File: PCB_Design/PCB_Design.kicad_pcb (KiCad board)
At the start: 2 copper layers, 1 part, among them IC1 ESP32-WROOM-32_M103QH3200PH3Q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

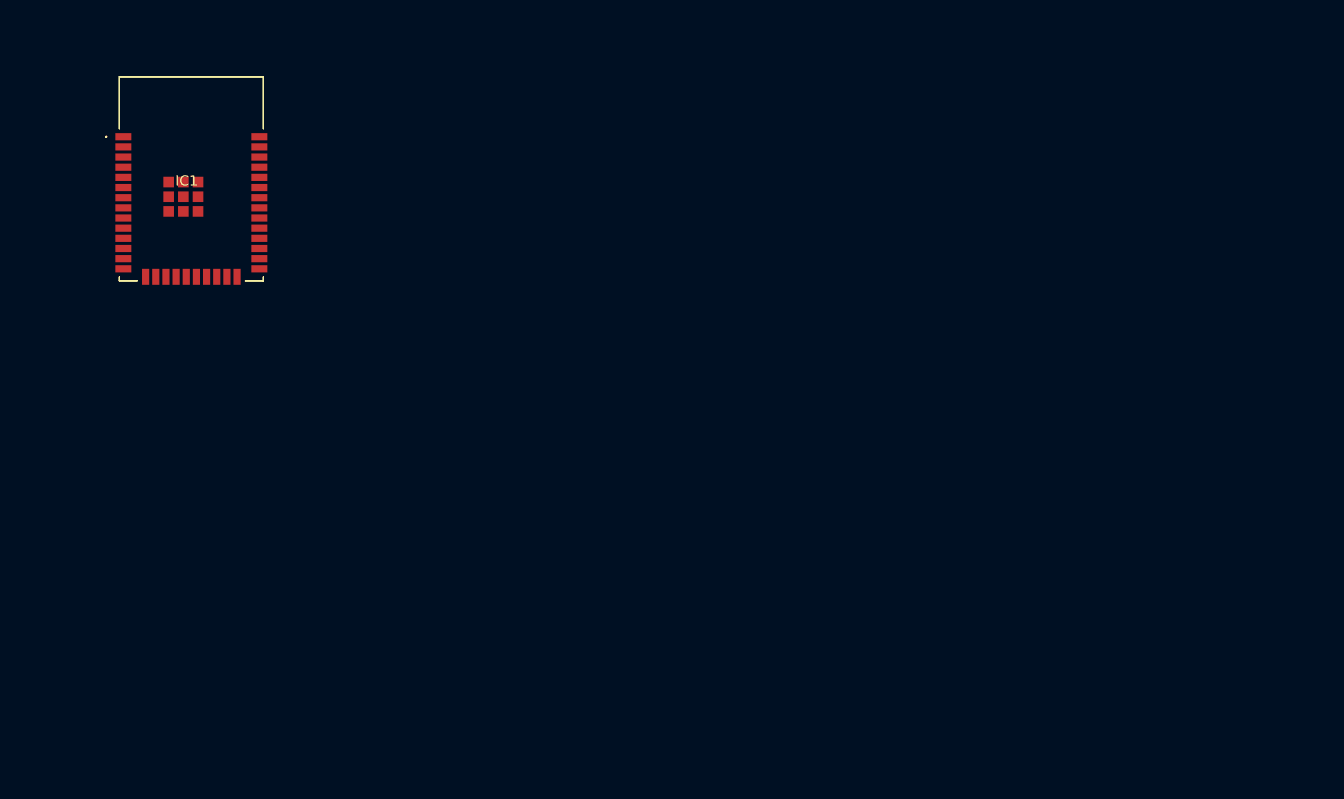
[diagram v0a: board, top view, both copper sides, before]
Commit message: huellas agregadas
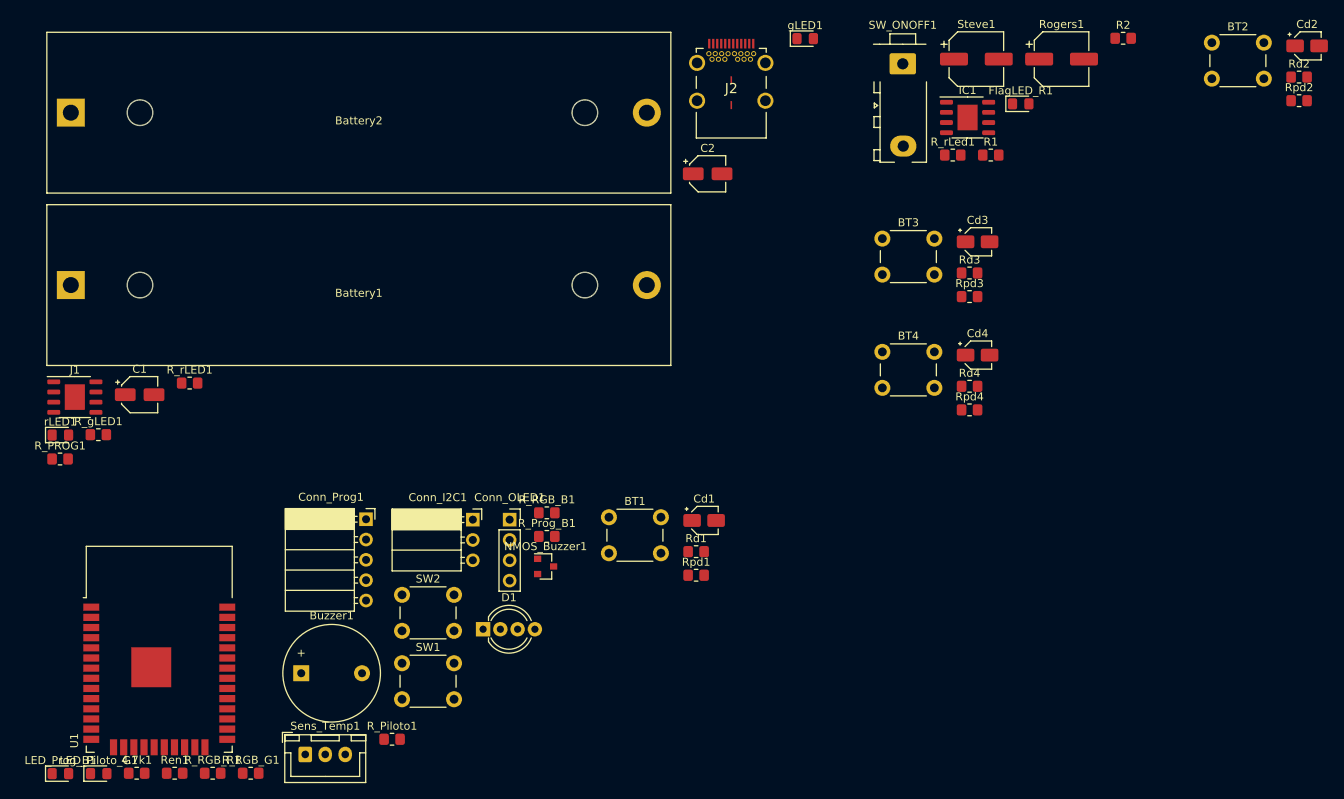
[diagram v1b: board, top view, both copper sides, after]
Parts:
- added 4.7k1: R_OneWire, Resistor_SMD:R_0805_2012Metric_Pad1.20x1.40mm_HandSolder, F.Cu at (92.2, 141.6)
- added BT1: SW_Push, Button_Switch_THT:SW_PUSH_6mm_H9.5mm, F.Cu at (151.3, 109.6)
- added BT2: SW_Push, Button_Switch_THT:SW_PUSH_6mm_H9.5mm, F.Cu at (226.6, 50.3)
- added BT3: SW_Push, Button_Switch_THT:SW_PUSH_6mm_H9.5mm, F.Cu at (185.4, 74.8)
- added BT4: SW_Push, Button_Switch_THT:SW_PUSH_6mm_H9.5mm, F.Cu at (185.4, 88.9)
- added Battery1: Battery_Cell, Battery:BatteryHolder_MPD_BH-18650-PC2, F.Cu at (84.0, 80.6)
- added Battery2: Battery_Cell, Battery:BatteryHolder_MPD_BH-18650-PC2, F.Cu at (84.0, 59.0)
- added Buzzer1: Buzzer, Buzzer_Beeper:Buzzer_12x9.5RM7.6, F.Cu at (112.8, 129.1)
- added C1: 10u, Capacitor_SMD:CP_Elec_4x5.8, F.Cu at (92.6, 94.3)
- added C2: 10u, Capacitor_SMD:CP_Elec_4x5.8, F.Cu at (163.6, 66.7)
- added Cd1: 1u, Capacitor_SMD:CP_Elec_3x5.4, F.Cu at (163.2, 110.0)
- added Cd2: 1u, Capacitor_SMD:CP_Elec_3x5.4, F.Cu at (238.5, 50.7)
- added Cd3: 1u, Capacitor_SMD:CP_Elec_3x5.4, F.Cu at (197.3, 75.2)
- added Cd4: 1u, Capacitor_SMD:CP_Elec_3x5.4, F.Cu at (197.3, 89.3)
- added Conn_I2C1: Conn_01x03_Female, Connector_PinSocket_2.54mm:PinSocket_1x03_P2.54mm_Horizontal, F.Cu at (134.2, 109.9)
- added Conn_OLED1: Conn_01x04_Female, Connector_PinSocket_2.54mm:PinSocket_1x04_P2.54mm_Vertical, F.Cu at (138.8, 109.9)
- added Conn_Prog1: Conn_01x05_Male, Connector_PinSocket_2.54mm:PinSocket_1x05_P2.54mm_Horizontal, F.Cu at (120.9, 109.9)
- added D1: LED_RGBC, LED_THT:LED_D5.0mm-4_RGB_Wide_Pins, F.Cu at (135.5, 123.6)
- added FlagLED_R1: LED, LED_SMD:LED_0805_2012Metric_Pad1.15x1.40mm_HandSolder, F.Cu at (202.7, 57.9)
- added J1: TP4056, Package_SO:SOIC-8-1EP_3.9x4.9mm_P1.27mm_EP2.514x3.2mm, F.Cu at (84.5, 94.6)
- added J2: 632723300011, 632723300011, F.Cu at (166.5, 56.3)
- added LED_Piloto_G1: LED, LED_SMD:LED_0805_2012Metric_Pad1.15x1.40mm_HandSolder, F.Cu at (87.5, 141.7)
- added LED_Prog_B1: LED, LED_SMD:LED_0805_2012Metric_Pad1.15x1.40mm_HandSolder, F.Cu at (82.7, 141.7)
- added NMOS_Buzzer1: Q_NMOS_GSD, Package_TO_SOT_SMD:SOT-23, F.Cu at (143.3, 115.8)
- added R1: 1M, Resistor_SMD:R_0805_2012Metric_Pad1.20x1.40mm_HandSolder, F.Cu at (199.0, 64.3)
- added R2: 590k, Resistor_SMD:R_0805_2012Metric_Pad1.20x1.40mm_HandSolder, F.Cu at (215.5, 49.7)
- added R_PROG1: R, Resistor_SMD:R_0805_2012Metric_Pad1.20x1.40mm_HandSolder, F.Cu at (82.6, 102.3)
- added R_Piloto1: 180, Resistor_SMD:R_0805_2012Metric_Pad1.20x1.40mm_HandSolder, F.Cu at (124.1, 137.4)
- added R_Prog_B1: 47, Resistor_SMD:R_0805_2012Metric_Pad1.20x1.40mm_HandSolder, F.Cu at (143.5, 112.0)
- added R_RGB_B1: 47, Resistor_SMD:R_0805_2012Metric_Pad1.20x1.40mm_HandSolder, F.Cu at (143.5, 109.1)
- added R_RGB_G1: 47, Resistor_SMD:R_0805_2012Metric_Pad1.20x1.40mm_HandSolder, F.Cu at (106.5, 141.6)
- added R_RGB_R1: 180, Resistor_SMD:R_0805_2012Metric_Pad1.20x1.40mm_HandSolder, F.Cu at (101.7, 141.6)
- added R_gLED1: 1k, Resistor_SMD:R_0805_2012Metric_Pad1.20x1.40mm_HandSolder, F.Cu at (87.4, 99.3)
- added R_rLED1: 1k, Resistor_SMD:R_0805_2012Metric_Pad1.20x1.40mm_HandSolder, F.Cu at (98.8, 92.8)
- added R_rLed1: 270, Resistor_SMD:R_0805_2012Metric_Pad1.20x1.40mm_HandSolder, F.Cu at (194.2, 64.3)
- added Rd1: 1k, Resistor_SMD:R_0805_2012Metric_Pad1.20x1.40mm_HandSolder, F.Cu at (162.2, 113.9)
- added Rd2: 1k, Resistor_SMD:R_0805_2012Metric_Pad1.20x1.40mm_HandSolder, F.Cu at (237.5, 54.6)
- added Rd3: 1k, Resistor_SMD:R_0805_2012Metric_Pad1.20x1.40mm_HandSolder, F.Cu at (196.3, 79.1)
- added Rd4: 1k, Resistor_SMD:R_0805_2012Metric_Pad1.20x1.40mm_HandSolder, F.Cu at (196.3, 93.2)
- added Ren1: 10k, Resistor_SMD:R_0805_2012Metric_Pad1.20x1.40mm_HandSolder, F.Cu at (97.0, 141.6)
- added Rogers1: 47u, Capacitor_SMD:CP_Elec_6.3x5.9, F.Cu at (207.8, 52.3)
- added Rpd1: 10k, Resistor_SMD:R_0805_2012Metric_Pad1.20x1.40mm_HandSolder, F.Cu at (162.2, 116.9)
- added Rpd2: 10k, Resistor_SMD:R_0805_2012Metric_Pad1.20x1.40mm_HandSolder, F.Cu at (237.5, 57.5)
- added Rpd3: 10k, Resistor_SMD:R_0805_2012Metric_Pad1.20x1.40mm_HandSolder, F.Cu at (196.3, 82.0)
- added Rpd4: 10k, Resistor_SMD:R_0805_2012Metric_Pad1.20x1.40mm_HandSolder, F.Cu at (196.3, 96.2)
- added SW1: SW_Push, Button_Switch_THT:SW_PUSH_6mm_H5mm, F.Cu at (125.4, 127.9)
- added SW2: SW_Push, Button_Switch_THT:SW_PUSH_6mm_H5mm, F.Cu at (125.4, 119.3)
- added SW_ONOFF1: SW_Push, Connector_TE-Connectivity:TE_MATE-N-LOK_1-770866-x_1x02_P4.14mm_Vertical, F.Cu at (188.1, 58.1)
- added Sens_Temp1: DS18B20, Connector_JST:JST_XH_B3B-XH-A_1x03_P2.50mm_Vertical, F.Cu at (113.3, 139.3)
- added Steve1: 47u, Capacitor_SMD:CP_Elec_6.3x5.9, F.Cu at (197.2, 52.3)
- added U1: ESP32-WROOM-32, RF_Module:ESP32-WROOM-32, F.Cu at (95.0, 129.1)
- added gLED1: LED, LED_SMD:LED_0805_2012Metric_Pad1.15x1.40mm_HandSolder, F.Cu at (175.8, 49.8)
- added rLED1: LED, LED_SMD:LED_0805_2012Metric_Pad1.15x1.40mm_HandSolder, F.Cu at (82.7, 99.3)
- IC1: value ESP32-WROOM-32_M103QH3200PH3Q0_ -> MIC37303YME; footprint ESP32-WROOM-32_M103QH3200PH3Q0:ESP32WROOM32M103QH3200PH3Q0 -> Package_SO:SOIC-8-1EP_3.9x4.9mm_P1.27mm_EP2.514x3.2mm
- moved IC1 97.3 mm to (196.1, 59.6)
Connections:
- IC1 pad 1: Net-(IC1-Pad1) -> GND
- IC1 pad 2: Net-(IC1-Pad2) -> Net-(FlagLED_R1-Pad2)
- IC1 pad 3: Net-(IC1-Pad3) -> Net-(FlagLED_R1-Pad2)
- IC1 pad 4: Net-(IC1-Pad4) -> Net-(FlagLED_R1-Pad2)
- IC1 pad 5: Net-(IC1-Pad5) -> /3.3v
- IC1 pad 6: Net-(IC1-Pad6) -> /3.3v
- IC1 pad 9: Net-(IC1-Pad9) -> GND

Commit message: huellas editadas
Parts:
- removed Conn_Prog1: Conn_01x05_Male, Connector_PinSocket_2.54mm:PinSocket_1x05_P2.54mm_Horizontal
- added Conn_prog1: Conn_01x05_Female, Connector_PinSocket_2.54mm:PinSocket_1x05_P2.54mm_Horizontal, F.Cu at (72.9, 103.8)
- J2: footprint 632723300011 -> Connector_USB:632723300011
- moved Cd1 48.4 mm to (115.2, 103.9)
- moved Conn_I2C1 48.4 mm to (86.2, 103.8)
- moved D1 48.4 mm to (87.5, 117.5)
- moved R_Prog_B1 48.4 mm to (95.5, 105.9)
- moved R_RGB_B1 48.4 mm to (95.5, 103.0)
- moved Rd1 48.4 mm to (114.2, 107.8)
- moved Rpd1 48.4 mm to (114.2, 110.8)
- moved C1 48.4 mm to (44.6, 88.2)
- moved LED_Prog_B1 48.4 mm to (34.7, 135.6)
- moved R_rLED1 48.4 mm to (50.8, 86.7)
- moved rLED1 48.4 mm to (34.7, 93.2)
- moved 4.7k1 48.4 mm to (44.2, 135.5)
- moved BT1 48.4 mm to (103.3, 103.5)
- moved BT2 48.4 mm to (178.6, 44.2)
- moved BT3 48.4 mm to (137.4, 68.7)
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
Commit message: Cambio del footprint de los porta baterias
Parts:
- Battery1, Battery2: moved to B.Cu
- moved LED_Prog_B1 426.9 mm to (450.9, 40.6)
- moved LED_Piloto_G1 420.5 mm to (450.9, 48.3)
- moved Ren1 404.4 mm to (450.9, 90.2)
- moved 4.7k1 394.5 mm to (438.4, 120.7)
- moved Conn_prog1 393.7 mm to (458.5, 24.1)
- moved U1 383.0 mm to (421.6, 43.2)
- moved R_Piloto1 376.4 mm to (443.2, 48.3)
- moved SW2 371.0 mm to (444.5, 59.7)
- moved SW1 370.8 mm to (444.5, 69.8)
- moved Sens_Temp1 367.8 mm to (433.1, 132.1)
- moved R_Prog_B1 353.8 mm to (443.2, 40.6)
- moved Cd1 275.6 mm to (390.7, 107.7)
- moved Rd1 275.6 mm to (389.7, 111.6)
- moved Rpd1 275.6 mm to (389.7, 114.6)
- moved BT1 275.2 mm to (378.5, 106.7)
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
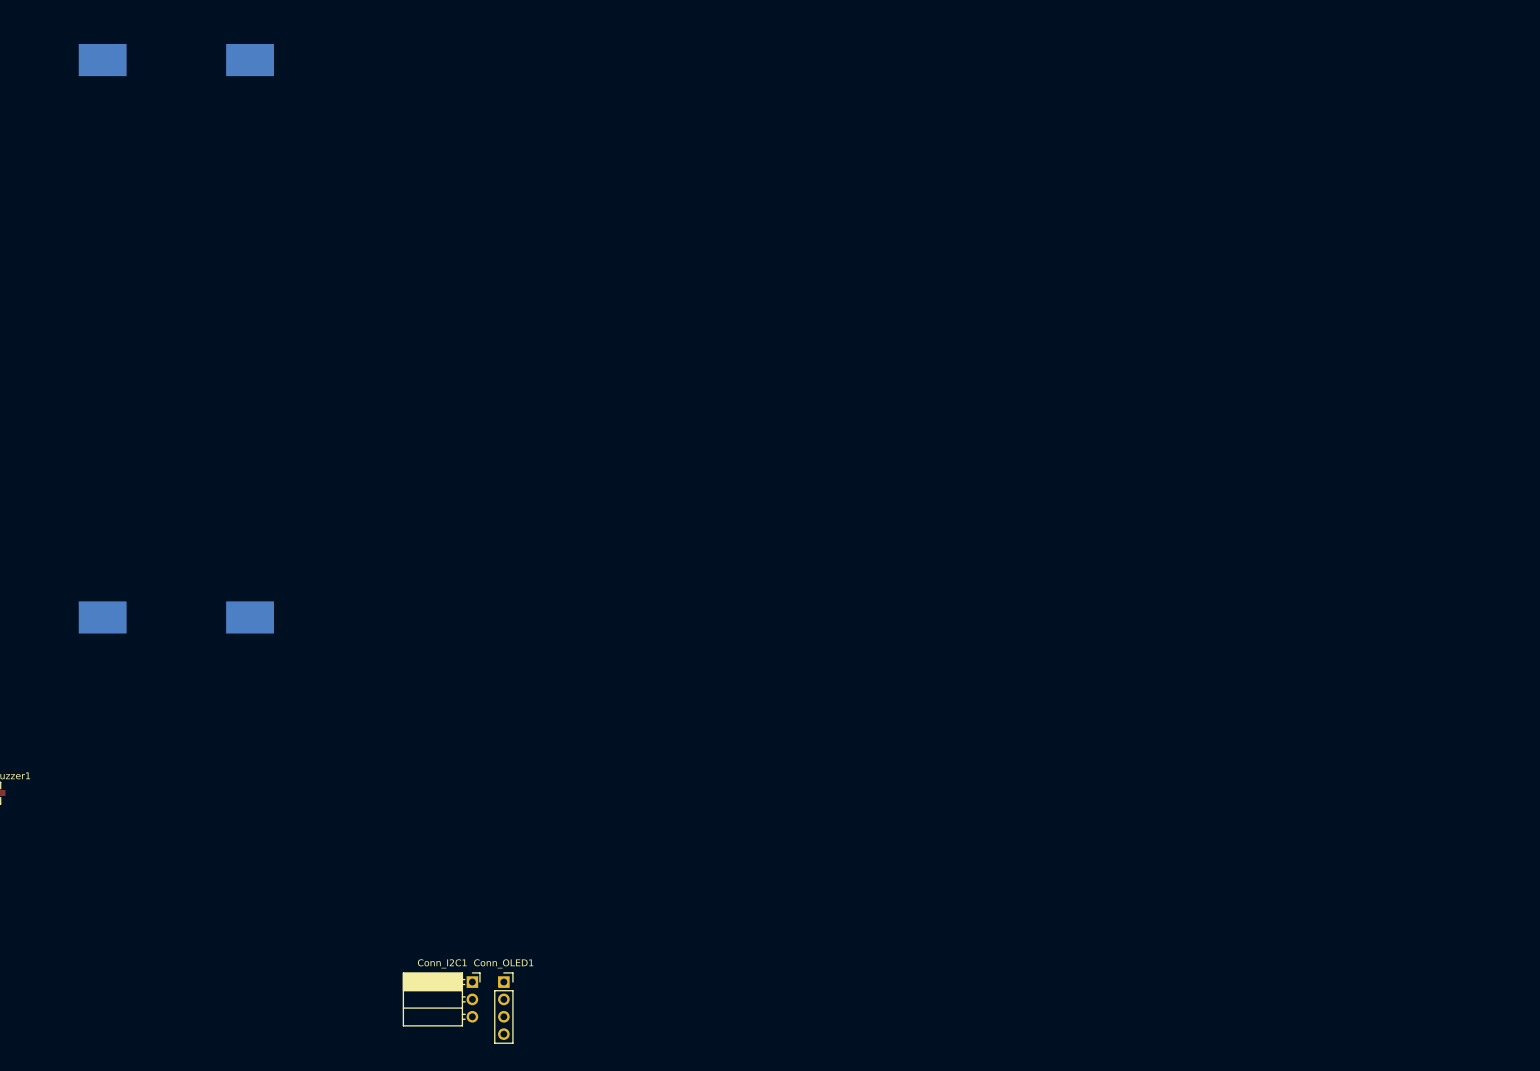
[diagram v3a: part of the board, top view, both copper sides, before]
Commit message: LCD footprint modified
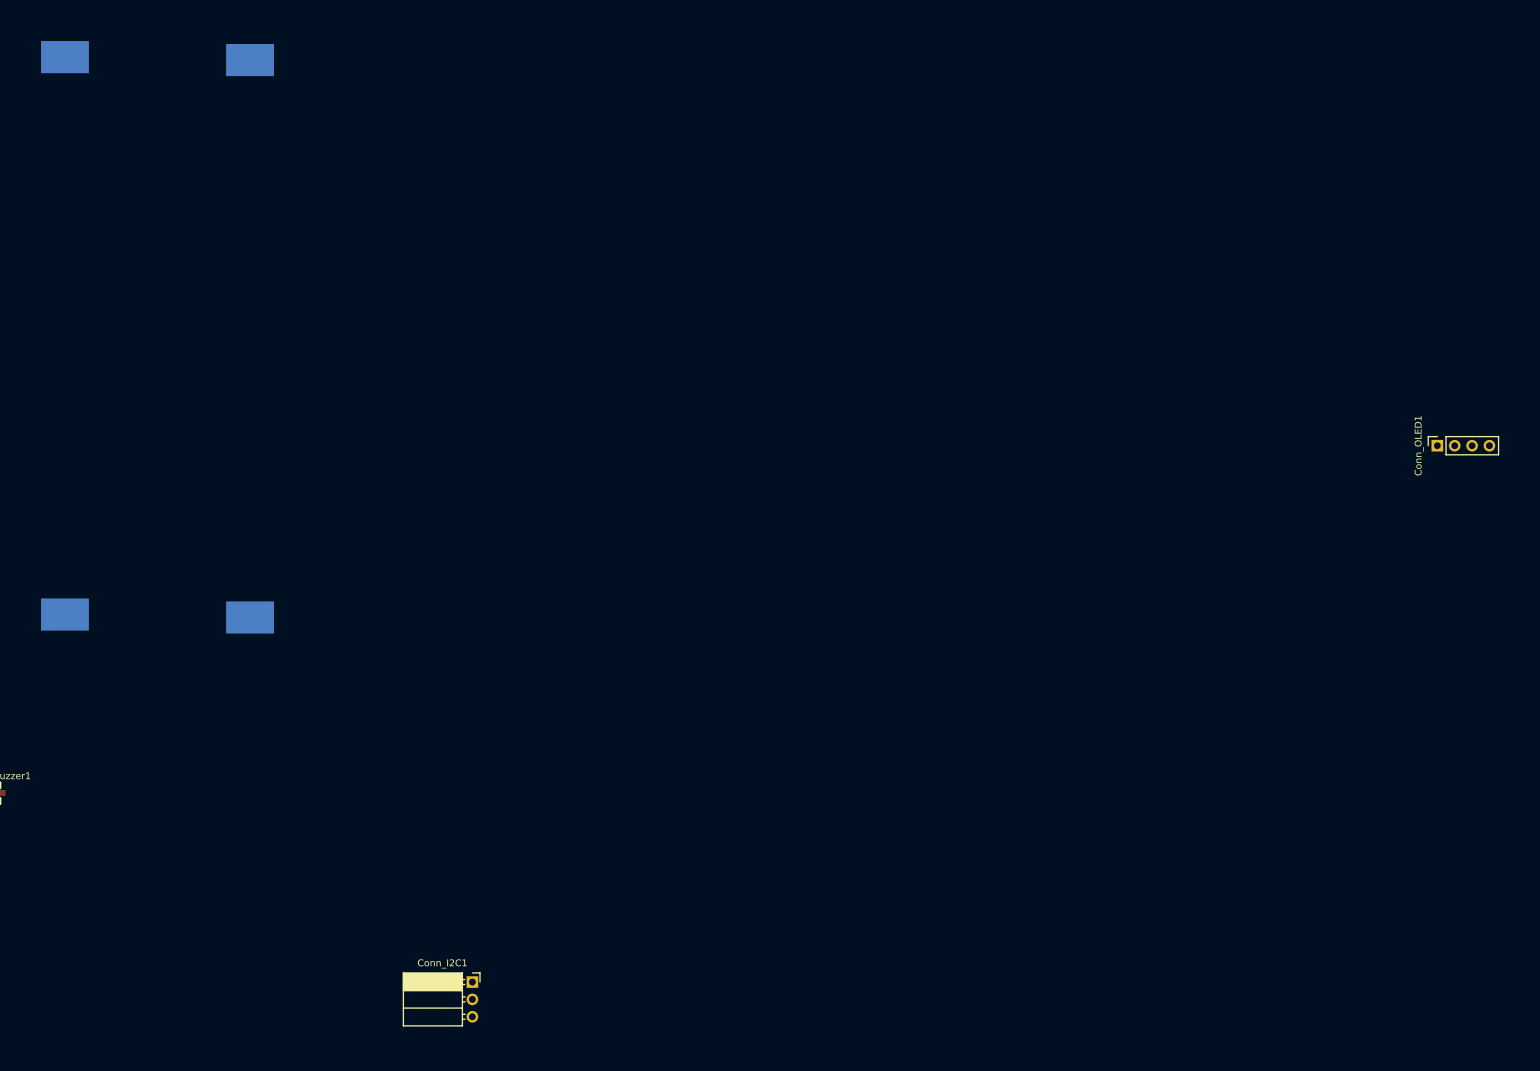
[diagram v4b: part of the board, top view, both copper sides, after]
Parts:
- moved Conn_OLED1 157.4 mm to (82.5, 110.5), turned to 90 degrees
- moved Battery1 5.53 mm to (-118.1, 58.4)

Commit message: Falta tetris
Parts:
- moved Cd4 332.5 mm to (65.5, 137.7), turned to 90 degrees
- moved Rd4 327.2 mm to (69.4, 138.7), turned to 90 degrees
- moved BT4 324.9 mm to (65.7, 154.7), turned to 90 degrees
- moved Rpd4 323.7 mm to (72.3, 138.7), turned to 90 degrees
- moved Cd3 317.8 mm to (78.0, 137.7), turned to 90 degrees
- moved LED_Piloto_G1 316.6 mm to (139.7, 106.7), turned to 270 degrees
- moved LED_Prog_B1 312.8 mm to (149.9, 125.7), turned to 270 degrees
- moved Rd3 312.5 mm to (81.9, 138.7), turned to 90 degrees
- moved Conn_prog1 310.0 mm to (160.0, 108.0), turned to 180 degrees
- moved BT3 309.6 mm to (78.2, 154.7), turned to 90 degrees
- moved Rpd3 309.1 mm to (84.8, 138.7), turned to 90 degrees
- moved R_Piloto1 307.8 mm to (139.7, 99.1), turned to 270 degrees
- moved R_Prog_B1 303.4 mm to (149.9, 118.1), turned to 270 degrees
- moved Cd2 302.7 mm to (91.6, 137.1), turned to 90 degrees
- moved D1 301.1 mm to (139.7, 123.8), turned to 90 degrees
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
